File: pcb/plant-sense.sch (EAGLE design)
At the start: 78 parts, among them CON1 2P-PH-TOP, CON2 3P-SH-TOP, CON3 3P-SH-TOP, CON4 3P-SH-TOP, CON5 3P-SH-TOP, CON6 4P-SH-TOP, CON7 4P-SH-TOP, CON8 4P-SH-TOP, CON9 4P-SH-TOP, T1 BC817, U1 MCP1253-33X50, U2 MIC23155, U3 FS312F-G, U4 FS8205, U5 EFM32PG1B200F256GM32, U6 SST26VF016B, U7 RFM69HW, U8 SI7021, U9 LTC4316, X1 40MHz

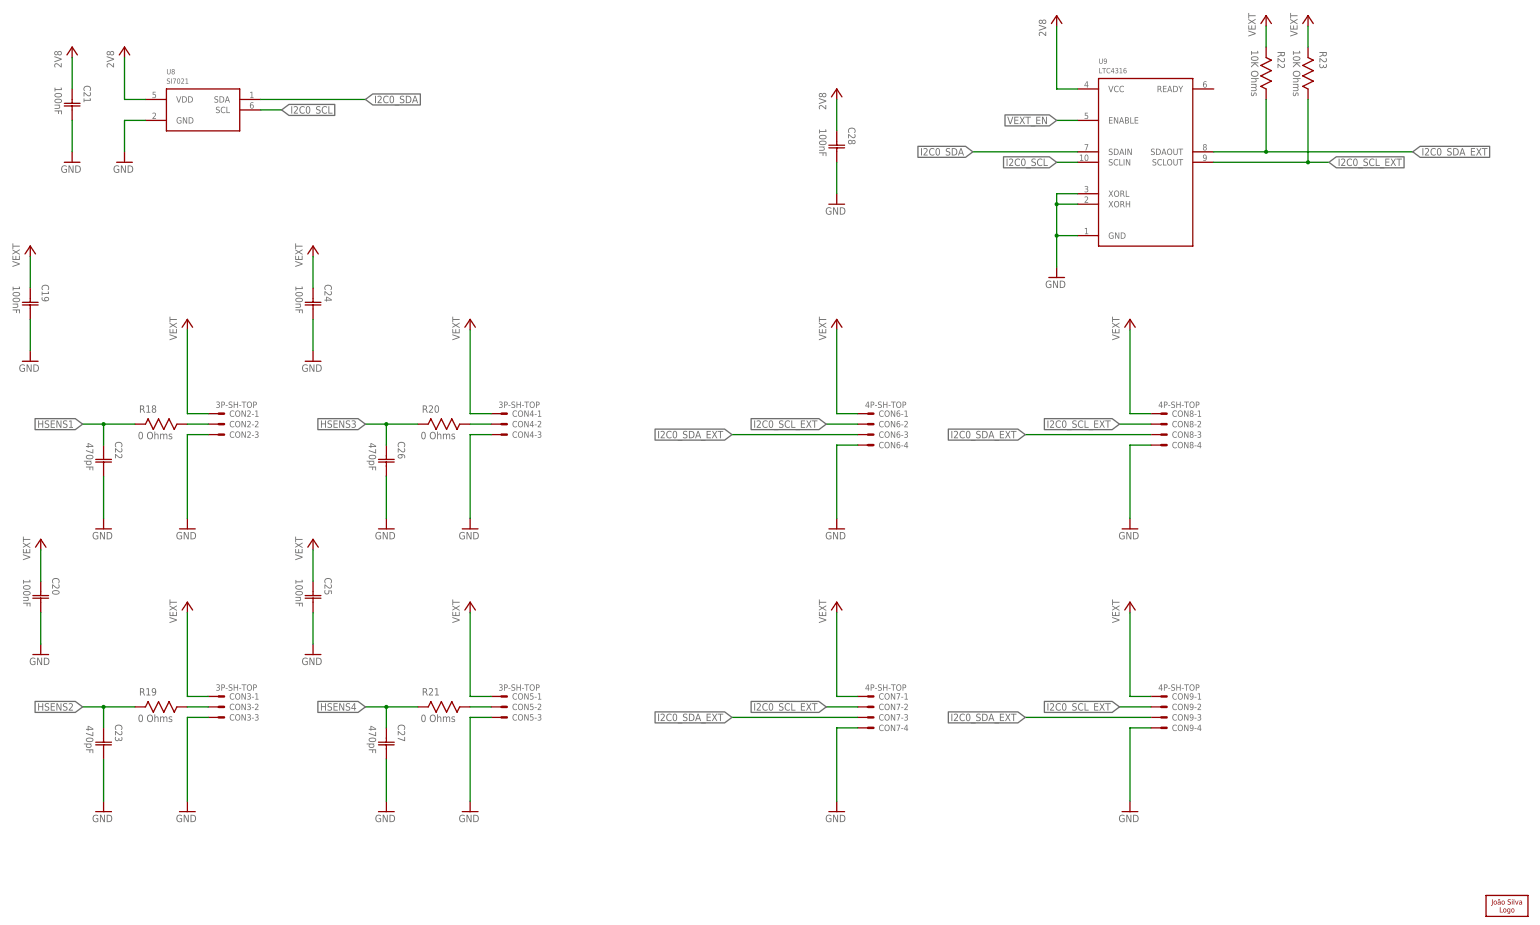
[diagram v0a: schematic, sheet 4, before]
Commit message: Sync library updates Add schematic PDF
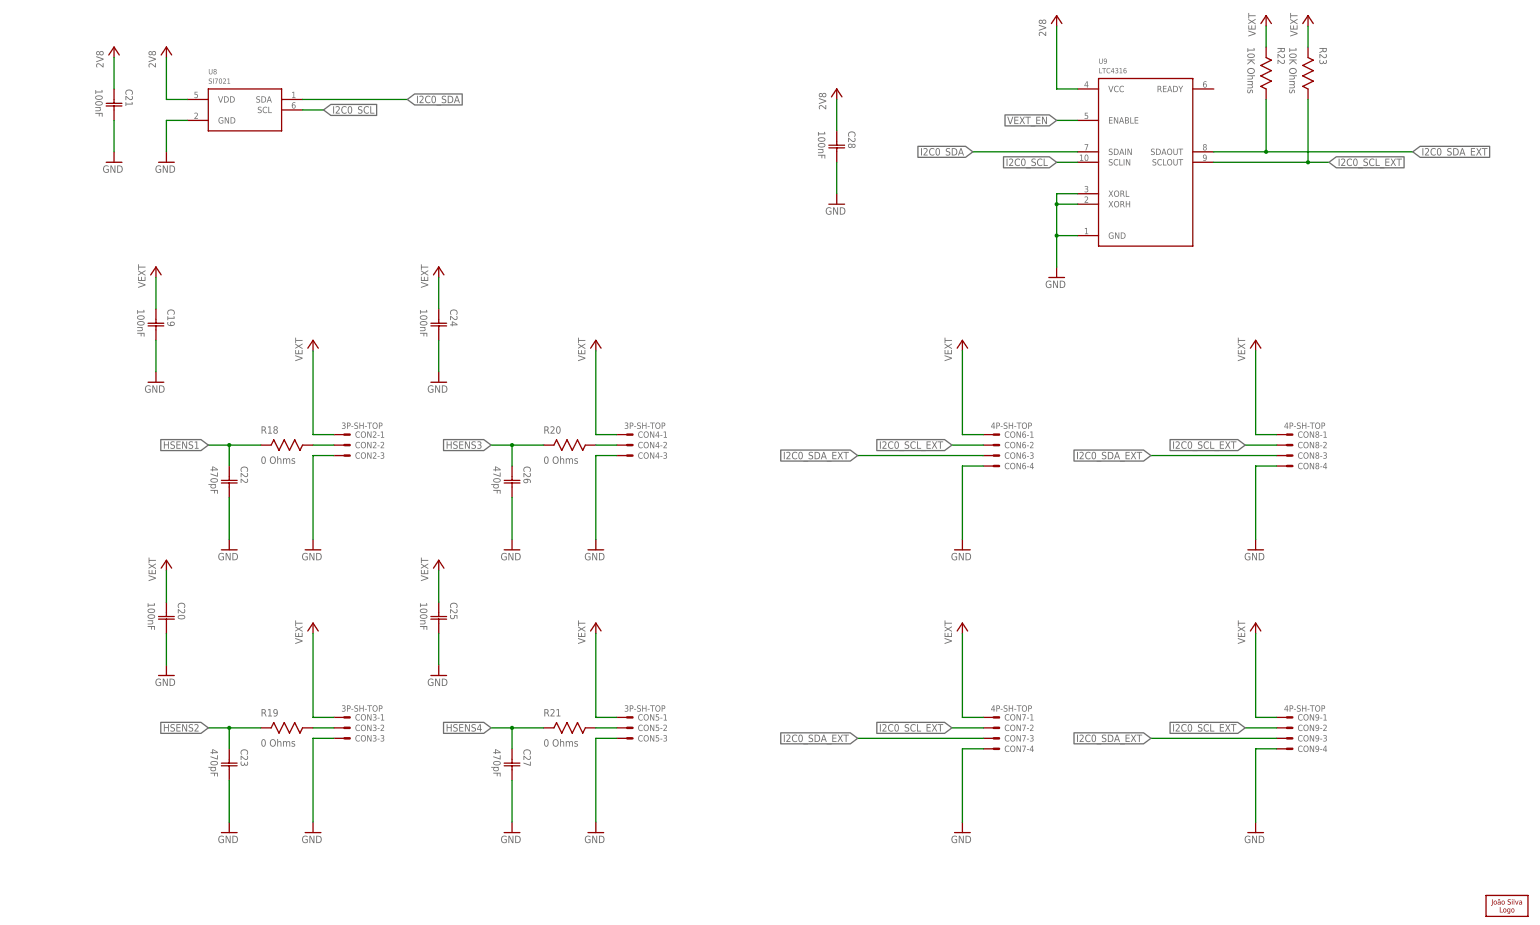
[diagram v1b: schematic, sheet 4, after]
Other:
- moved on the sheet: C19, C20, C21, C22, C23, C24, C25, C26, C27, CON2-1, CON2-2, CON2-3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
